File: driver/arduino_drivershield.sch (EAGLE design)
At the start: 37 parts, among them IC1 LB1973M, IC10 LB1973M, IC11 LB1973M, IC12 74HC14D, IC2 LB1973M, IC3 74HC14D, IC4 LB1973M, IC5 LB1973M, IC6 74HC14D, IC7 LB1973M, IC8 LB1973M, IC9 74HC14D, U1 ARDUINO_SHIELDLABEL

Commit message: maybe now all my old follies are fixed?
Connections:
- net FOO: no longer SJ1.1
- net GND@PWR: now also SJ1.1
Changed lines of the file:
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@@
-</segment>
-<segment>
-<pinref part="GND9" gate="1" pin="GNDA"/>
-<wire x1="-15.24" y1="15.24" x2="-15.24" y2="17.78" width="0.1524" layer="91"/>
-<pinref part="SJ1" gate="1" pin="1"/>
 </segment>
 <segment>
@@
 <wire x1="60.96" y1="-12.7" x2="58.42" y2="-10.16" width="0.1524" layer="91"/>
 </segment>
+<segment>
+<pinref part="GND9" gate="1" pin="GNDA"/>
+<wire x1="-15.24" y1="15.24" x2="-15.24" y2="17.78" width="0.1524" layer="91"/>
+<pinref part="SJ1" gate="1" pin="1"/>
+</segment>
 </net>

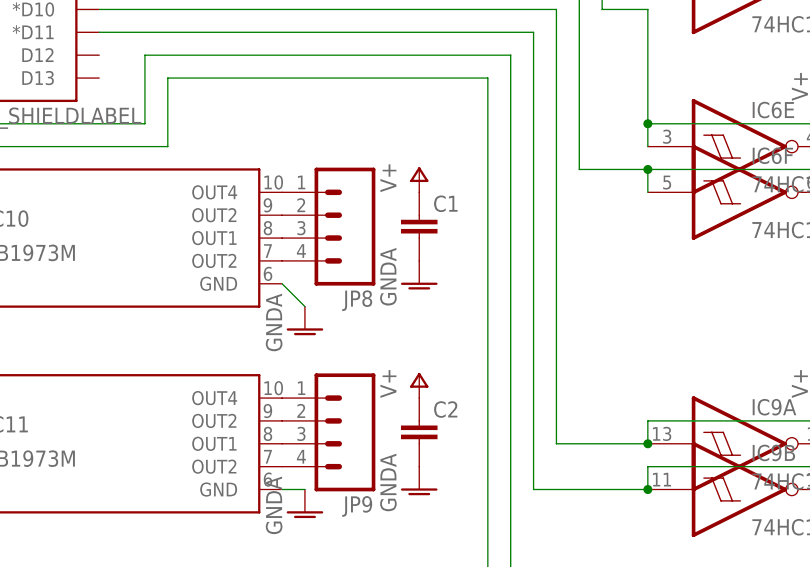
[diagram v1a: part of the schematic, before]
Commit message: maybe now all my old follies are fixed?
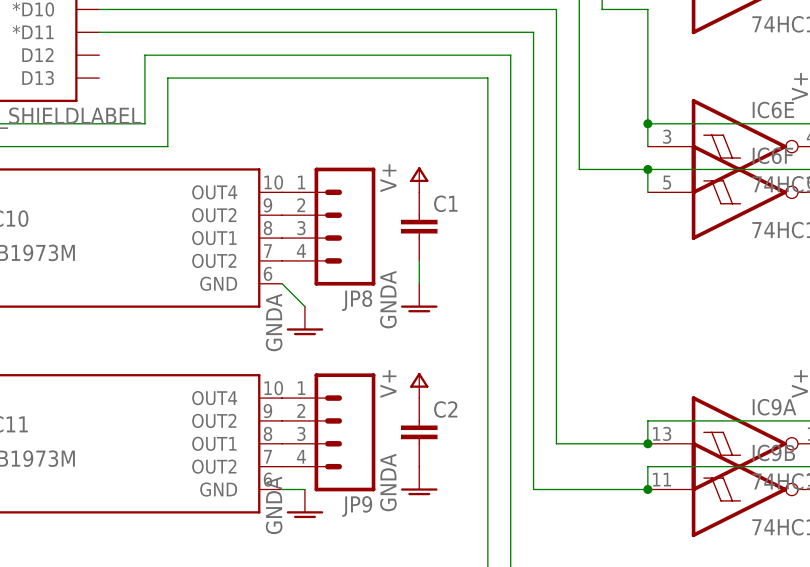
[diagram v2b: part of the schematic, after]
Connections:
- removed net FOO: C1.2, C2.2, C3.2, C4.2, C5.2, C6.2, C7.2, C8.2, IC1.GND, IC11.GND, IC2.GND, IC4.GND, IC5.GND, IC7.GND, IC8.GND, SJ3.1, SJ4.1
- net GND@PWR: now also C1.2, C2.2, C3.2, C4.2, C5.2, C6.2, C7.2, C8.2, IC1.GND, IC11.GND, IC2.GND, IC4.GND, IC5.GND, IC7.GND, IC8.GND, SJ3.1, SJ4.1
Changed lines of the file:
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@@
 <instance part="P+14" gate="1" x="193.04" y="-43.18"/>
 <instance part="GND21" gate="1" x="73.66" y="-33.02"/>
-<instance part="GND22" gate="1" x="73.66" y="-10.16"/>
+<instance part="GND22" gate="1" x="73.66" y="-12.7"/>
 <instance part="P+15" gate="1" x="73.66" y="-20.32"/>
 <instance part="P+16" gate="1" x="73.66" y="2.54"/>
@@
 </segment>
 </net>
-<net name="FOO" class="1">
-<segment>
-<pinref part="IC8" gate="G$1" pin="GND"/>
-<pinref part="GND7" gate="1" pin="GNDA"/>
-<wire x1="182.88" y1="-58.42" x2="180.34" y2="-55.88" width="0.1524" layer="91"/>
-</segment>
-<segment>
-<pinref part="IC7" gate="G$1" pin="GND"/>
-<pinref part="GND2" gate="1" pin="GNDA"/>
-</segment>
-<segment>
-<pinref part="IC5" gate="G$1" pin="GND"/>
-<pinref part="GND4" gate="1" pin="GNDA"/>
-</segment>
-<segment>
-<pinref part="IC4" gate="G$1" pin="GND"/>
-<pinref part="GND3" gate="1" pin="GNDA"/>
-</segment>
-<segment>
-<pinref part="IC2" gate="G$1" pin="GND"/>
-<pinref part="GND5" gate="1" pin="GNDA"/>
-</segment>
-<segment>
-<pinref part="IC1" gate="G$1" pin="GND"/>
-<pinref part="GND8" gate="1" pin="GNDA"/>
-</segment>
-<segment>
-<pinref part="C8" gate="G$1" pin="2"/>
-<pinref part="GND15" gate="1" pin="GNDA"/>
-</segment>
-<segment>
-<pinref part="C7" gate="G$1" pin="2"/>
-<pinref part="GND16" gate="1" pin="GNDA"/>
-</segment>
-<segment>
-<pinref part="C6" gate="G$1" pin="2"/>
-<pinref part="GND17" gate="1" pin="GNDA"/>
-</segment>
-<segment>
-<pinref part="C5" gate="G$1" pin="2"/>
-<pinref part="GND18" gate="1" pin="GNDA"/>
-</segment>
-<segment>
-<pinref part="C4" gate="G$1" pin="2"/>
-<pinref part="GND19" gate="1" pin="GNDA"/>
-</segment>
-<segment>
-<pinref part="C3" gate="G$1" pin="2"/>
-<pinref part="GND20" gate="1" pin="GNDA"/>
-</segment>
-<segment>
-<pinref part="C2" gate="G$1" pin="2"/>
-<pinref part="GND21" gate="1" pin="GNDA"/>
-</segment>
-<segment>
-<pinref part="C1" gate="G$1" pin="2"/>
-<pinref part="GND22" gate="1" pin="GNDA"/>
-</segment>
-<segment>
-<pinref part="IC11" gate="G$1" pin="GND"/>
-<wire x1="60.96" y1="-33.02" x2="58.42" y2="-33.02" width="0.1524" layer="91"/>
-<pinref part="GND14" gate="1" pin="GNDA"/>
-</segment>
-<segment>
-<pinref part="GND23" gate="1" pin="GNDA"/>
-<wire x1="-7.62" y1="27.94" x2="-5.08" y2="27.94" width="0.1524" layer="91"/>
-<pinref part="SJ3" gate="1" pin="1"/>
-</segment>
-<segment>
-<pinref part="GND24" gate="1" pin="GNDA"/>
-<wire x1="-7.62" y1="38.1" x2="-5.08" y2="38.1" width="0.1524" layer="91"/>
-<pinref part="SJ4" gate="1" pin="1"/>
-</segment>
-</net>
 <net name="GND" class="0">
 <segment>
@@
 <pinref part="SJ1" gate="1" pin="1"/>
 </segment>
-</net>
+<segment>
+<pinref part="IC8" gate="G$1" pin="GND"/>
+<pinref part="GND7" gate="1" pin="GNDA"/>
+<wire x1="182.88" y1="-58.42" x2="180.34" y2="-55.88" width="0.1524" layer="91"/>
+</segment>
+<segment>
+<pinref part="IC7" gate="G$1" pin="GND"/>
+<pinref part="GND2" gate="1" pin="GNDA"/>
+</segment>
+<segment>
+<pinref part="IC5" gate="G$1" pin="GND"/>
+<pinref part="GND4" gate="1" pin="GNDA"/>
+</segment>
+<segment>
+<pinref part="IC4" gate="G$1" pin="GND"/>
+<pinref part="GND3" gate="1" pin="GNDA"/>
+</segment>
+<segment>
+<pinref part="IC2" gate="G$1" pin="GND"/>
+<pinref part="GND5" gate="1" pin="GNDA"/>
+</segment>
+<segment>
+<pinref part="IC1" gate="G$1" pin="GND"/>
+<pinref part="GND8" gate="1" pin="GNDA"/>
+</segment>
+<segment>
+<pinref part="C8" gate="G$1" pin="2"/>
+<pinref part="GND15" gate="1" pin="GNDA"/>
+</segment>
+<segment>
+<pinref part="C7" gate="G$1" pin="2"/>
+<pinref part="GND16" gate="1" pin="GNDA"/>
+</segment>
+<segment>
+<pinref part="C6" gate="G$1" pin="2"/>
+<pinref part="GND17" gate="1" pin="GNDA"/>
+</segment>
+<segment>
+<pinref part="C5" gate="G$1" pin="2"/>
+<pinref part="GND18" gate="1" pin="GNDA"/>
+</segment>
+<segment>
+<pinref part="C4" gate="G$1" pin="2"/>
+<pinref part="GND19" gate="1" pin="GNDA"/>
+</segment>
+<segment>
+<pinref part="C3" gate="G$1" pin="2"/>
+<pinref part="GND20" gate="1" pin="GNDA"/>
+</segment>
+<segment>
+<pinref part="C2" gate="G$1" pin="2"/>
+<pinref part="GND21" gate="1" pin="GNDA"/>
+</segment>
+<segment>
+<pinref part="C1" gate="G$1" pin="2"/>
+<pinref part="GND22" gate="1" pin="GNDA"/>
+<wire x1="73.66" y1="-10.16" x2="73.66" y2="-7.62" width="0.1524" layer="91"/>
+</segment>
+<segment>
+<pinref part="IC11" gate="G$1" pin="GND"/>
+<wire x1="60.96" y1="-33.02" x2="58.42" y2="-33.02" width="0.1524" layer="91"/>
+<pinref part="GND14" gate="1" pin="GNDA"/>
+</segment>
+<segment>
+<pinref part="GND23" gate="1" pin="GNDA"/>
+<wire x1="-7.62" y1="27.94" x2="-5.08" y2="27.94" width="0.1524" layer="91"/>
+<pinref part="SJ3" gate="1" pin="1"/>
+</segment>
+<segment>
+<pinref part="GND24" gate="1" pin="GNDA"/>
+<wire x1="-7.62" y1="38.1" x2="-5.08" y2="38.1" width="0.1524" layer="91"/>
+<pinref part="SJ4" gate="1" pin="1"/>
+</segment>
+</net>

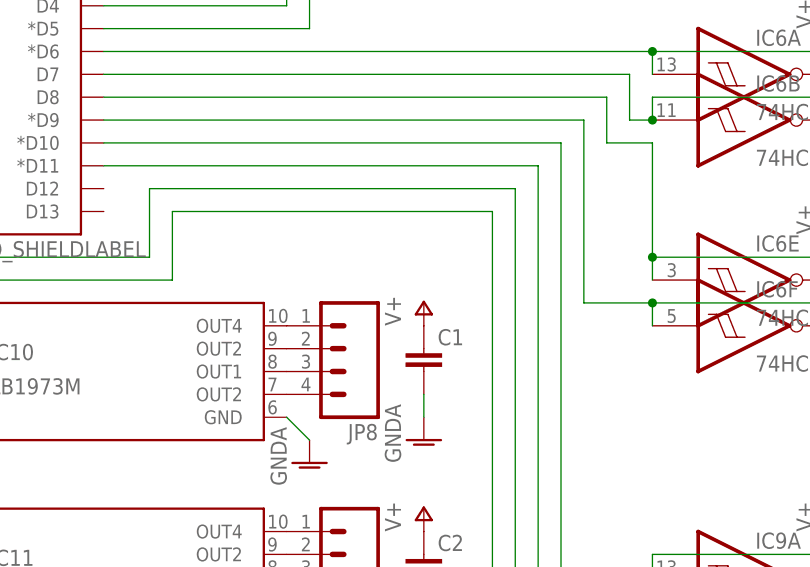
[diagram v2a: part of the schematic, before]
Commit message: added via to get more ground coverage
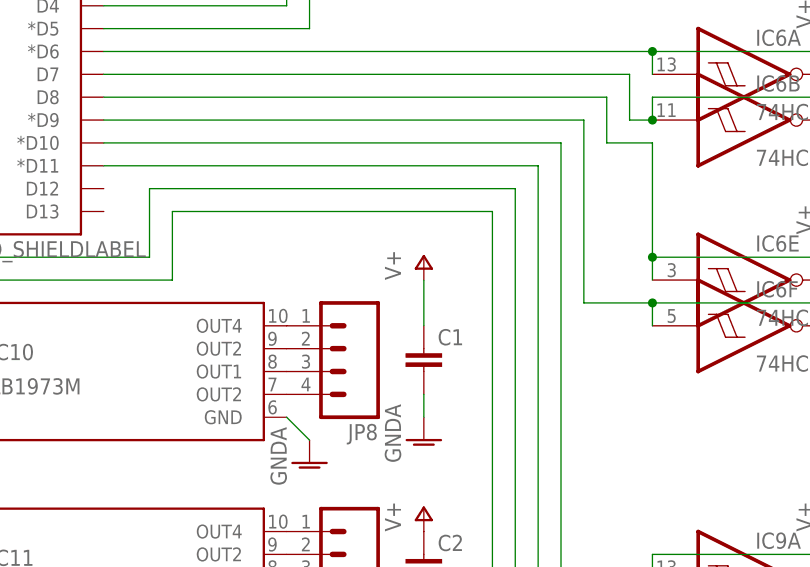
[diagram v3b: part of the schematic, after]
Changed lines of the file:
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@@
 <instance part="GND22" gate="1" x="73.66" y="-12.7"/>
 <instance part="P+15" gate="1" x="73.66" y="-20.32"/>
-<instance part="P+16" gate="1" x="73.66" y="2.54"/>
+<instance part="P+16" gate="1" x="73.66" y="7.62"/>
 <instance part="GND9" gate="1" x="-15.24" y="12.7"/>
 <instance part="C9" gate="G$1" x="58.42" y="109.22"/>
@@
 <pinref part="C1" gate="G$1" pin="1"/>
 <pinref part="P+16" gate="1" pin="V+"/>
-</segment>
-</net>
+<wire x1="73.66" y1="5.08" x2="73.66" y2="0" width="0.1524" layer="91"/>
+</segment>
+</net>

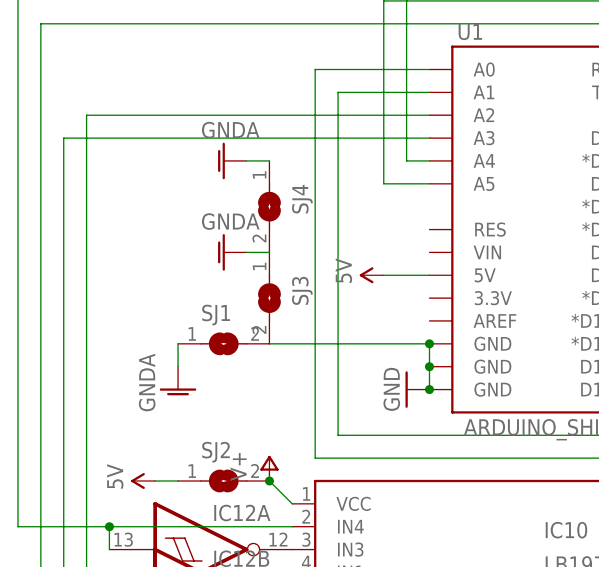
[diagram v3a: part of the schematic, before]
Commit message: added one more low-ESR cap
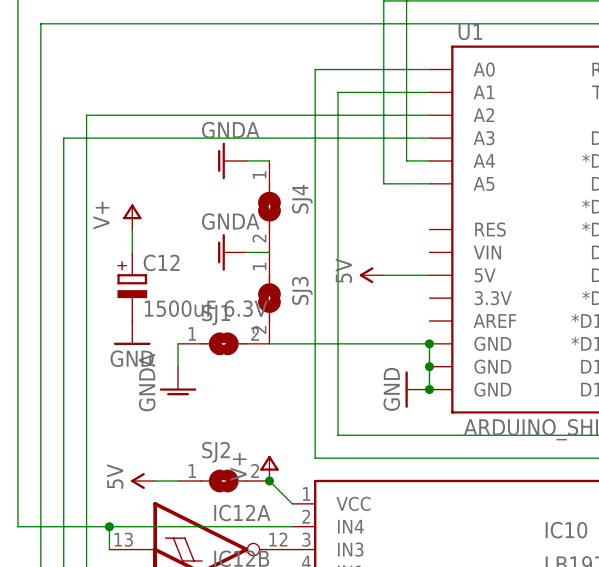
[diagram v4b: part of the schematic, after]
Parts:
- added C12: 1500uF 6.3V, rcl:CPOL-EUE5-10.5
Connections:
- new net GNDA: SJ1.1
- net GND: now also C12.-
- net GND@PWR: no longer SJ1.1
- net V+: now also C12.+
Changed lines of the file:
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@@
 <part name="GND24" library="supply1" deviceset="GNDA" device=""/>
 <part name="SJ4" library="jumper" deviceset="SJ" device=""/>
+<part name="C12" library="rcl" deviceset="CPOL-EU" device="E5-10.5" value="1500uF 6.3V"/>
+<part name="P+17" library="supply1" deviceset="V+" device=""/>
+<part name="GND25" library="SparkFun-Aesthetics" deviceset="GND" device=""/>
 </parts>
 <sheets>
@@
 <instance part="GND24" gate="1" x="-10.16" y="38.1" rot="R270"/>
 <instance part="SJ4" gate="1" x="-5.08" y="33.02" rot="R270"/>
+<instance part="C12" gate="G$1" x="-20.32" y="25.4"/>
+<instance part="P+17" gate="1" x="-20.32" y="33.02"/>
+<instance part="GND25" gate="1" x="-20.32" y="17.78"/>
 </instances>
 <busses>
@@
 <wire x1="73.66" y1="5.08" x2="73.66" y2="0" width="0.1524" layer="91"/>
 </segment>
+<segment>
+<pinref part="C12" gate="G$1" pin="+"/>
+<pinref part="P+17" gate="1" pin="V+"/>
+<wire x1="-20.32" y1="27.94" x2="-20.32" y2="30.48" width="0.1524" layer="91"/>
+</segment>
 </net>
 <net name="GND" class="0">
@@
 <junction x="165.1" y="124.46"/>
 </segment>
+<segment>
+<pinref part="C12" gate="G$1" pin="-"/>
+<pinref part="GND25" gate="1" pin="GND"/>
+</segment>
 </net>
 <net name="5V" class="0">
@@
 </segment>
 <segment>
-<pinref part="GND9" gate="1" pin="GNDA"/>
-<wire x1="-15.24" y1="15.24" x2="-15.24" y2="17.78" width="0.1524" layer="91"/>
-<pinref part="SJ1" gate="1" pin="1"/>
-</segment>
-<segment>
 <pinref part="IC8" gate="G$1" pin="GND"/>
 <pinref part="GND7" gate="1" pin="GNDA"/>
@@
 </segment>
 </net>
+<net name="GNDA" class="0">
+<segment>
+<pinref part="SJ1" gate="1" pin="1"/>
+<pinref part="GND9" gate="1" pin="GNDA"/>
+<wire x1="-15.24" y1="17.78" x2="-15.24" y2="15.24" width="0.1524" layer="91"/>
+</segment>
+</net>

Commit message: seems I messed up the net name here at some point, now corrected
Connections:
- removed net GNDA: SJ1.1
- net GND@PWR: now also SJ1.1
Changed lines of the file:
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@@
 <pinref part="SJ4" gate="1" pin="1"/>
 </segment>
-</net>
-<net name="GNDA" class="0">
 <segment>
 <pinref part="SJ1" gate="1" pin="1"/>
